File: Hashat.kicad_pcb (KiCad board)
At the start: 2 copper layers, 65 x 56.5 mm, 101 parts, among them IC1 BM1397_mode1, J1 Raspberry_Pi_2_3, J2 Conn_01x04, J3 Conn_01x05, J4 PJ-202AH, U1 EMC2101, U10 SN74AXC1T45DBVR, U3 DS4432U+, U4 25MHz, U5 SN74AXC1T45DBVR, U6 MCP1824T-1802E, U7 MCP1824T-0802E, U8 SN74AXC1T45DBVR, U9 SN74AXC1T45DBVR

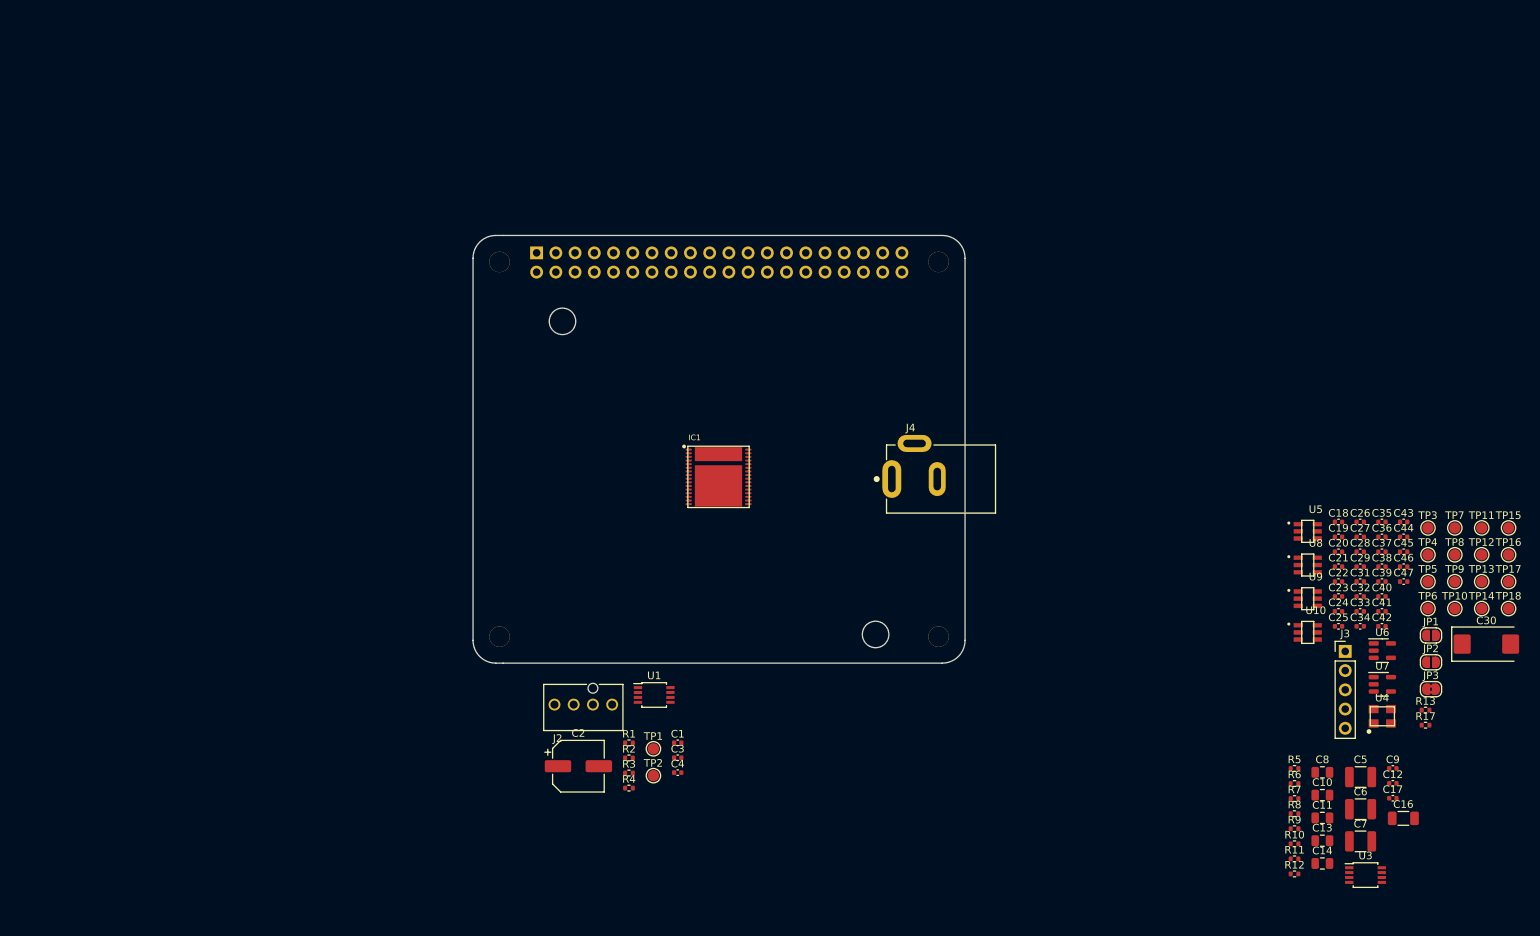
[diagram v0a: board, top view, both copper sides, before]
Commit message: cleared up some part reference designator madness
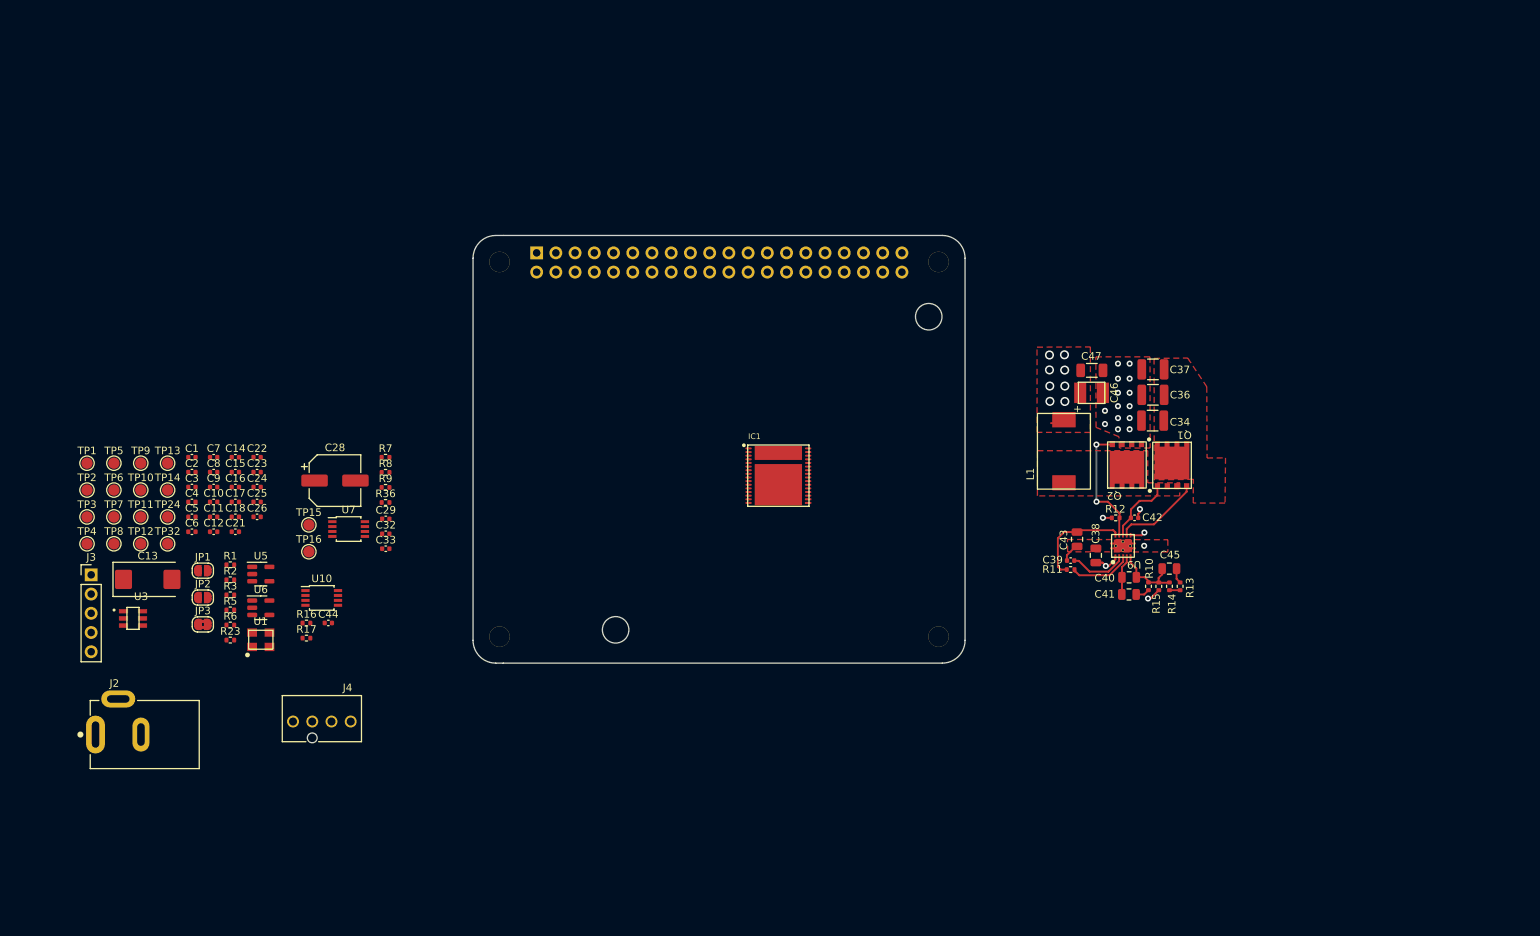
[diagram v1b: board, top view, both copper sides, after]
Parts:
- removed C19, C20, C27, C31, C35: 587-5514-1-ND, Capacitor_SMD:C_0402_1005Metric
- removed C30: 330uF, Capacitor_Tantalum_SMD:CP_EIA-7343-31_Kemet-D_Pad2.25x2.55mm_HandSolder
- removed R4: 10k, Resistor_SMD:R_0402_1005Metric
- removed TP17, TP18: TestPoint, TestPoint:TestPoint_Pad_D1.5mm
- removed U4: 25MHz, bitaxe:O 25,0-JO32-B-1V3-1-T1-LF
- removed U8: SN74AXC1T45DBVR, bitaxe:SN74AXC1T45
- added C15: 587-5514-1-ND, Capacitor_SMD:C_0402_1005Metric, F.Cu at (45.6, 86.8)
- added L1: 150nH, TPS40305_supply:FP1005R1-R15-R, F.Cu at (155.1, 84.0)
- added Q1: CSD17311Q5, TPS40305_supply:CSD17311Q5, F.Cu at (169.3, 85.9)
- added Q2: CSD17311Q5, TPS40305_supply:CSD17311Q5, F.Cu at (163.4, 85.8)
- added R14: 4.99k, Resistor_SMD:R_0402_1005Metric, F.Cu at (169.0, 101.9)
- added R15: 3.32k, Resistor_SMD:R_0402_1005Metric, F.Cu at (167.6, 101.9)
- added R16: 80k, Resistor_SMD:R_0402_1005Metric, F.Cu at (55.0, 106.7)
- added R23: 0, Resistor_SMD:R_0402_1005Metric, F.Cu at (44.9, 109.0)
- added R36: 10k, Resistor_SMD:R_0402_1005Metric, F.Cu at (65.4, 90.8)
- added TP24: TestPoint, TestPoint:TestPoint_Pad_D1.5mm, F.Cu at (36.7, 92.7)
- added TP32: TestPoint, TestPoint:TestPoint_Pad_D1.5mm, F.Cu at (36.7, 96.2)
- C1: value 470pF -> 311-3342-1-ND
- C10: value 180pF -> 587-5514-1-ND; footprint Capacitor_SMD:C_0805_2012Metric -> Capacitor_SMD:C_0402_1005Metric
- C11: value 1.5nF -> 587-5514-1-ND; footprint Capacitor_SMD:C_0805_2012Metric -> Capacitor_SMD:C_0402_1005Metric
- C12: value 0.1uF -> 587-5514-1-ND
- C13: value 10uF -> 330uF; footprint Capacitor_SMD:C_0805_2012Metric -> Capacitor_Tantalum_SMD:CP_EIA-7343-31_Kemet-D_Pad2.25x2.55mm_HandSolder
- C14: value 470pF -> 587-5514-1-ND; footprint Capacitor_SMD:C_0805_2012Metric -> Capacitor_SMD:C_0402_1005Metric
- C16: value 100uF -> 587-5514-1-ND; footprint Capacitor_SMD:C_1206_3216Metric -> Capacitor_SMD:C_0402_1005Metric
- C17: value 1uF -> 587-5514-1-ND
- C18, C3, C4: value 311-3342-1-ND -> 587-5514-1-ND
- C2: value 220uF -> 587-5514-1-ND; footprint Capacitor_SMD:CP_Elec_6.3x7.7 -> Capacitor_SMD:C_0402_1005Metric
- C21, C22, C23, C29, C33: value 587-5514-1-ND -> 311-3342-1-ND
- C24, C44: value 311-3342-1-ND -> 1uF
- C25: value 587-5514-1-ND -> 1uF
- C28: value 587-5514-1-ND -> 220uF; footprint Capacitor_SMD:C_0402_1005Metric -> Capacitor_SMD:CP_Elec_6.3x7.7
- C32: value 587-5514-1-ND -> 470pF
- C34: value 587-5514-1-ND -> 47uF; footprint Capacitor_SMD:C_0402_1005Metric -> Capacitor_SMD:C_1210_3225Metric
- C36, C37: value 311-3342-1-ND -> 47uF; footprint Capacitor_SMD:C_0402_1005Metric -> Capacitor_SMD:C_1210_3225Metric
- C38: value 311-3342-1-ND -> 1uF; footprint Capacitor_SMD:C_0402_1005Metric -> Capacitor_SMD:C_0805_2012Metric
- C39: value 311-3342-1-ND -> 3.3nF
- C40: value 1uF -> 180pF; footprint Capacitor_SMD:C_0402_1005Metric -> Capacitor_SMD:C_0805_2012Metric
- C41: value 1uF -> 1.5nF; footprint Capacitor_SMD:C_0402_1005Metric -> Capacitor_SMD:C_0805_2012Metric
- C42: value 311-3342-1-ND -> 0.1uF
- C43: value 311-3342-1-ND -> 10uF; footprint Capacitor_SMD:C_0402_1005Metric -> Capacitor_SMD:C_0805_2012Metric
- C45: value 311-3342-1-ND -> 470pF; footprint Capacitor_SMD:C_0402_1005Metric -> Capacitor_SMD:C_0805_2012Metric
- C46: value 311-3342-1-ND -> 220uF; footprint Capacitor_SMD:C_0402_1005Metric -> TPS40305_supply:CAP_2R5TPE220MAFB
- C47: value 311-3342-1-ND -> 100uF; footprint Capacitor_SMD:C_0402_1005Metric -> Capacitor_SMD:C_1206_3216Metric
- C5, C6: value 47uF -> 587-5514-1-ND; footprint Capacitor_SMD:C_1210_3225Metric -> Capacitor_SMD:C_0402_1005Metric
- C7: value 47uF -> 311-3342-1-ND; footprint Capacitor_SMD:C_1210_3225Metric -> Capacitor_SMD:C_0402_1005Metric
- C8: value 1uF -> 587-5514-1-ND; footprint Capacitor_SMD:C_0805_2012Metric -> Capacitor_SMD:C_0402_1005Metric
- C9: value 3.3nF -> 311-3342-1-ND
- J2: value Conn_01x04 -> PJ-202AH; footprint bitaxe:470531000 -> bitaxe:CUI_PJ-202AH
- J4: value PJ-202AH -> Conn_01x04; footprint bitaxe:CUI_PJ-202AH -> bitaxe:470531000
- R1: value 100 -> 1k
- R10: value 3.32k -> 3.83k
- R11: value 80k -> 100k
- R12: value DNP -> 4.12k
- R13: value 1k -> 1.33k
- R17: value 10k -> DNP
- R2: value 100 -> 0
- R3: value 10k -> 0
- R5: value 3.83k -> 0
- R6: value 100k -> 10k
- R7: value 4.12k -> 100
- R8: value 1.33k -> 100
- R9: value 4.99k -> 10k
- U1: value EMC2101 -> 25MHz; footprint Package_SO:TSSOP-8_3x3mm_P0.65mm -> bitaxe:O 25,0-JO32-B-1V3-1-T1-LF
- U10: value SN74AXC1T45DBVR -> DS4432U+; footprint bitaxe:SN74AXC1T45 -> Package_SO:TSSOP-8_3x3mm_P0.65mm
- U3: value DS4432U+ -> SN74AXC1T45DBVR; footprint Package_SO:TSSOP-8_3x3mm_P0.65mm -> bitaxe:SN74AXC1T45
- U5: value SN74AXC1T45DBVR -> MCP1824T-1802E; footprint bitaxe:SN74AXC1T45 -> Package_TO_SOT_SMD:SOT-23-5
- U6: value MCP1824T-1802E -> MCP1824T-0802E
- U7: value MCP1824T-0802E -> EMC2101; footprint Package_TO_SOT_SMD:SOT-23-5 -> Package_SO:TSSOP-8_3x3mm_P0.65mm
- U9: value SN74AXC1T45DBVR -> TPS40305; footprint bitaxe:SN74AXC1T45 -> TPS40305_supply:TPS40305
- moved TP11 177.2 mm to (33.1, 92.7)
- moved TP12 177.2 mm to (33.1, 96.2)
- moved TP3 177.2 mm to (26.0, 92.7)
- moved TP4 177.2 mm to (26.0, 96.2)
- moved TP7 177.2 mm to (29.6, 92.7)
- moved TP8 177.2 mm to (29.6, 96.2)
- moved TP13 174.3 mm to (36.7, 85.6)
- moved TP14 174.3 mm to (36.7, 89.1)
- moved TP5 174.3 mm to (29.6, 85.6)
- moved TP6 174.3 mm to (29.6, 89.1)
- moved TP10 174.3 mm to (33.1, 89.1)
- moved TP9 174.3 mm to (33.1, 85.6)
- moved U3 166.3 mm to (32.1, 106.1)
- moved J3 166.0 mm to (26.6, 100.3)
- moved JP1 162.5 mm to (41.3, 99.8)
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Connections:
- C1 pad 1: Net-(U1-DP) -> GND
- C1 pad 2: Net-(U1-DN) -> /BM1397/1V8
- C10 pad 1: Net-(U2-COMP) -> /BM1397/VDD
- C10 pad 2: /Power/OUT0 -> GND
- C11 pad 1: Net-(U2-COMP) -> /BM1397/VDD
- C11 pad 2: Net-(C11-Pad2) -> GND
- C12 pad 1: Net-(U2-BOOT) -> /BM1397/VDD
- C12 pad 2: /Power/SW -> Net-(IC1-VDD3_1)
- C13 pad 1: Net-(U2-BP) -> /BM1397/VDD
- C14 pad 1: Net-(C14-Pad1) -> /BM1397/1V8
- C14 pad 2: /Power/OUT0 -> GND
- C16 pad 1: /BM1397/VDD -> /BM1397/0V8
- C17 pad 1: /3V3 -> Net-(IC1-VDD2_1)
- C17 pad 2: GND -> Net-(IC1-VDD1_1)
- C18 pad 1: GND -> Net-(IC1-VDD1_1)
- C18 pad 2: /BM1397/1V8 -> GND
- C2 pad 1: /5V -> GND
- C2 pad 2: GND -> Net-(IC1-VDD1_0)
- C21 pad 1: /BM1397/0V8 -> /BM1397/1V8
- C22 pad 1: /BM1397/1V8 -> /5V
- C23 pad 1: Net-(IC1-VDD2_0) -> /5V
- C23 pad 2: Net-(IC1-VDD3_0) -> GND
- C24 pad 1: /BM1397/VDD -> /BM1397/1V8
- C25 pad 1: Net-(IC1-VDD3_0) -> /BM1397/0V8
- C25 pad 2: /BM1397/VDD -> GND
- C26 pad 1: /BM1397/VDD -> /BM1397/3V3
- C28 pad 1: /BM1397/VDD -> /5V
- C29 pad 1: /BM1397/VDD -> /5V
- C29 pad 2: Net-(IC1-VDD3_1) -> GND
- C3 pad 1: /5V -> Net-(IC1-VDD1_0)
- C3 pad 2: GND -> Net-(IC1-VDD2_0)
- C32 pad 1: /BM1397/1V8 -> Net-(U7-DP)
- C32 pad 2: GND -> Net-(U7-DN)
- C33 pad 1: /BM1397/0V8 -> /3V3
- C34 pad 1: Net-(IC1-VDD2_1) -> /5V
- C34 pad 2: Net-(IC1-VDD1_1) -> GND
- C36 pad 1: /BM1397/1V8 -> /5V
- C37 pad 1: /BM1397/3V3 -> /5V
- C39 pad 1: /5V -> Net-(U9-SS)
- C4 pad 1: /3V3 -> /BM1397/0V8
- C40 pad 1: /BM1397/1V8 -> Net-(U9-COMP)
- C40 pad 2: GND -> /Power/OUT0
- C41 pad 1: /BM1397/0V8 -> Net-(U9-COMP)
- C41 pad 2: GND -> Net-(C41-Pad2)
- C42 pad 1: /BM1397/1V8 -> Net-(U9-BOOT)
- C42 pad 2: GND -> /Power/SW
- C43 pad 1: /BM1397/3V3 -> Net-(U9-BP)
- C44 pad 1: /BM1397/1V8 -> /3V3
- C45 pad 1: /BM1397/3V3 -> Net-(C45-Pad1)
- C45 pad 2: GND -> /Power/OUT0
- C46 pad 1: /BM1397/1V8 -> /BM1397/VDD
- C47 pad 1: /BM1397/3V3 -> /BM1397/VDD
- C5 pad 1: /5V -> /BM1397/1V8
- C6 pad 1: /5V -> Net-(IC1-VDD2_0)
- C6 pad 2: GND -> Net-(IC1-VDD3_0)
- C7 pad 1: /5V -> /BM1397/VDD
- C8 pad 1: /5V -> Net-(IC1-VDD3_0)
- C8 pad 2: GND -> /BM1397/VDD
- C9 pad 1: Net-(U2-SS) -> /BM1397/VDD
- IC1 pad 10: /BM1397/BM_RO -> Net-(IC1-RO)
- IC1 pad 11: /BM1397/BM_CI -> Net-(IC1-CI)
- IC1 pad 12: Net-(IC1-CLKI) -> /BM1397/BM_CLKI
- IC1 pad 9: /BM1397/BM_RST_N -> /BM1397/RST_N
- J1 pad 10: /BM1397/RO -> /RPi/RO
- J1 pad 11: /BM1397/RST -> /RPi/RST
- J1 pad 36: /BM1397/BI -> /RPi/BI
- J1 pad 8: /BM1397/CI -> /RPi/CI
- J2 pad 1: GND -> /5V
- J2 pad 2: /5V -> GND
- J2 pad 3: /Fan/FAN_TACH -> GND
- J4 pad 1: /5V -> GND
- J4 pad 2: GND -> /5V
- J4 pad 3: GND -> /Fan/FAN_TACH
- R1 pad 1: Net-(U1-DN) -> GND
- R1 pad 2: /BM1397/TEMP_N -> /BM1397/RST_N
- R10 pad 1: /Power/OUT0 -> Net-(C41-Pad2)
- R10 pad 2: GND -> /Power/OUT0
- R11 pad 1: Net-(U3-FS0) -> /Power/PGOOD
- R11 pad 2: GND -> Net-(U9-BP)
- R12 pad 1: Net-(U3-FS1) -> Net-(Q2-G)
- R13 pad 1: GND -> /BM1397/VDD
- R13 pad 2: /BM1397/BM_RST_N -> Net-(C45-Pad1)
- R17 pad 1: Net-(IC1-RI) -> Net-(U10-FS1)
- R17 pad 2: /BM1397/1V8 -> GND
- R2 pad 1: /BM1397/TEMP_P -> Net-(U1-OUT)
- R2 pad 2: Net-(U1-DP) -> /BM1397/BM_CLKI
- R3 pad 1: /Fan/FAN_TACH -> /BM1397/RO
- R3 pad 2: /3V3 -> Net-(IC1-RO)
- R5 pad 1: Net-(C11-Pad2) -> /BM1397/CI
- R5 pad 2: /Power/OUT0 -> Net-(IC1-CI)
- R6 pad 1: /Power/PGOOD -> Net-(IC1-RI)
- R6 pad 2: Net-(U2-BP) -> /BM1397/1V8
- R7 pad 1: Net-(Q2-G) -> Net-(U7-DN)
- R7 pad 2: GND -> /BM1397/TEMP_N
- R8 pad 1: /BM1397/VDD -> /BM1397/TEMP_P
- R8 pad 2: Net-(C14-Pad1) -> Net-(U7-DP)
- R9 pad 1: /BM1397/VDD -> /Fan/FAN_PWM
- R9 pad 2: /Power/OUT0 -> /3V3
- TP1 pad 1: /Fan/FAN_TACH -> Net-(U1-OUT)
- TP10 pad 1: Net-(IC1-NRSTO) -> Net-(IC1-PIN_MODE)
- TP11 pad 1: Net-(IC1-CO) -> /BM1397/TEMP_P
- TP12 pad 1: Net-(IC1-CLKO) -> /BM1397/TEMP_N
- TP13 pad 1: Net-(IC1-PIN_MODE) -> /BM1397/1V8
- TP14 pad 1: Net-(IC1-RI) -> /BM1397/0V8
- TP15 pad 1: /BM1397/TEMP_P -> /Fan/FAN_PWM
- TP16 pad 1: /BM1397/TEMP_N -> /Fan/FAN_TACH
- TP2 pad 1: /Fan/FAN_PWM -> /BM1397/CI
- TP3 pad 1: Net-(IC1-CLKI) -> /BM1397/RO
- TP4 pad 1: /BM1397/CI -> /BM1397/RST_N
- TP5 pad 1: /BM1397/RO -> GND
- TP6 pad 1: /BM1397/RST_N -> Net-(IC1-BO)
- TP7 pad 1: GND -> Net-(IC1-NRSTO)
- TP8 pad 1: /BM1397/BM_BI -> Net-(IC1-CO)
- TP9 pad 1: Net-(IC1-BO) -> Net-(IC1-CLKO)
- U1 pad 1: /3V3 -> /BM1397/1V8
- U1 pad 2: Net-(U1-DP) -> GND
- U1 pad 3: Net-(U1-DN) -> Net-(U1-OUT)
- U1 pad 4: /Fan/FAN_PWM -> /BM1397/1V8
- U10 pad 1: /BM1397/1V8 -> /Fan/SDA
- U10 pad 2: GND -> /Fan/SCL
- U10 pad 3: /BM1397/BM_BI -> Net-(U10-FS1)
- U10 pad 4: /BM1397/BI -> GND
- U10 pad 5: GND -> Net-(U10-FS0)
- U10 pad 6: /BM1397/3V3 -> /Power/OUT0
- U3 pad 1: /Fan/SDA -> /BM1397/1V8
- U3 pad 2: /Fan/SCL -> GND
- U3 pad 3: Net-(U3-FS1) -> Net-(U3-A)
- U3 pad 4: GND -> /BM1397/CLKI
- U3 pad 5: Net-(U3-FS0) -> GND
- U3 pad 6: /Power/OUT0 -> /BM1397/3V3
- U5 pad 1: /BM1397/1V8 -> /5V
- U5 pad 3: /BM1397/BM_RST_N -> /5V
- U5 pad 4: /BM1397/RST -> unconnected-(U5-PG-Pad4)
- U5 pad 5: GND -> /BM1397/1V8
- U6 pad 5: /BM1397/1V8 -> /BM1397/0V8
- U7 pad 1: /5V -> /3V3
- U7 pad 2: GND -> Net-(U7-DP)
- U7 pad 3: /5V -> Net-(U7-DN)
- U7 pad 4: unconnected-(U7-PG-Pad4) -> /Fan/FAN_PWM
- U7 pad 5: /BM1397/0V8 -> GND
- U9 pad 1: /BM1397/1V8 -> /5V
- U9 pad 2: GND -> Net-(U9-SS)
- U9 pad 3: /BM1397/BM_CI -> /Power/PGOOD
- U9 pad 4: /BM1397/CI -> Net-(U9-COMP)
- U9 pad 5: GND -> /Power/OUT0
- U9 pad 6: /BM1397/3V3 -> Net-(U9-BOOT)
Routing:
- net Net-(Q2-G): track 0.00 -> 16.3 mm, vias 0 -> 2
- net Net-(U9-BP): track 0.00 -> 13.6 mm
- net Net-(Q1-G): track 0.00 -> 11.5 mm
- net /Power/OUT0: track 0.00 -> 9.84 mm
- net /Power/SW: track 0.00 -> 9.30 mm
- net /Power/PGOOD: track 0.00 -> 8.53 mm
- net Net-(U9-SS): track 0.00 -> 7.78 mm
- net GND: track 0.00 -> 5.60 mm, vias 0 -> 17
- net Net-(U9-COMP): track 0.00 -> 5.29 mm
- net /5V: track 0.00 -> 3.50 mm, vias 0 -> 1
- net /BM1397/VDD: track 0.00 -> 3.36 mm
- net Net-(U9-BOOT): track 0.00 -> 3.22 mm, vias 0 -> 2
- net Net-(C45-Pad1): track 0.00 -> 2.03 mm
- net Net-(C41-Pad2): track 0.00 -> 1.86 mm
- net (no net): vias 0 -> 8
- added copper zone on F.Cu, net /5V
- added copper zone on F.Cu, net /BM1397/VDD
- added copper zone on F.Cu, net /Power/SW
- added copper zone on F.Cu, net GND

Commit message: swapped out the VCCIO LDOs for some LCSC versions
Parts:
- removed J2: PJ-202AH, bitaxe:CUI_PJ-202AH
- added DC1: DC-044K-D025, lcsc:DC-IN-TH_DC-044K-D025, F.Cu at (85.3, 68.1)
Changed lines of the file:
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@@
+    )
+  )
+  (footprint "lcsc:DC-IN-TH_DC-044K-D025" (layer "F.Cu")
+    (at 85.27 68.123)
+    (property "JLC Part" "Extended Part")
+    (property "LCSC Part" "C963204")
+    (property "Manufacturer" "G-Switch")
+    (property "Sheetfile" "/Users/skot/Work/Bitcoin/Hashat/Hashat.sch")
+    (property "Sheetname" "")
+    (attr smd)
+    (fp_text reference "DC1" (at 2.087 6.122) (layer "F.SilkS")
+        (effects (font (size 1 1) (thickness 0.15)))
+    )
+    (fp_text value "DC-044K-D025" (at 0 8.93) (layer "F.Fab")
+        (effects (font (size 1 1) (thickness 0.15)))
+    )
+    (fp_text user "${REFERENCE}" (at 0 0) (layer "F.Fab")
+        (effects (font (size 1 1) (thickness 0.15)))
+    )
+    (fp_line (start -8.28 -4.85) (end -7.36 -4.85)
+      (stroke (width 0.25) (type solid)) (layer "F.SilkS"))
+    (fp_line (start -8.28 -2.06) (end -8.28 -4.85)
+      (stroke (width 0.25) (type solid)) (layer "F.SilkS"))
+    (fp_line (start -8.28 -2.06) (end -8.28 1.11)
+      (stroke (width 0.25) (type solid)) (layer "F.SilkS"))
+    (fp_line (start -8.28 1.11) (end -8.28 4.93)
+      (stroke (width 0.25) (type solid)) (layer "F.SilkS"))
+    (fp_line (start -8.28 4.93) (end -7.36 4.93)
+      (stroke (width 0.25) (type solid)) (layer "F.SilkS"))
+    (fp_line (start -3.1 -4.85) (end 3.34 -4.85)
+      (stroke (width 0.25) (type solid)) (layer "F.SilkS"))
+    (fp_line (start -3.1 4.93) (end 3.34 4.93)
+      (stroke (width 0.25) (type solid)) (layer "F.SilkS"))
+    (fp_line (start 3.34 -4.85) (end 3.34 -4.24)
+      (stroke (width 0.25) (type solid)) (layer "F.SilkS"))
+    (fp_line (start 3.34 -3.41) (end 3.34 0.96)
+      (stroke (width 0.25) (type solid)) (layer "F.SilkS"))
+    (fp_line (start 3.34 1.79) (end 3.34 4.93)
+      (stroke (width 0.25) (type solid)) (layer "F.SilkS"))
+    (fp_circle (center 4.16 1.3) (end 4.31 1.3)
+      (stroke (width 0.3) (type solid)) (fill none) (layer "Cmts.User"))
+    (fp_circle (center -8.28 -5.12) (end -8.25 -5.12)
+      (stroke (width 0.06) (type solid)) (fill none) (layer "F.Fab"))
+    (fp_circle (center 5.23 1.2) (end 5.48 1.2)
+      (stroke (width 0.5) (type solid)) (fill none) (layer "F.Fab"))
+    (pad "" thru_hole circle (at -4.27 1.2) (size 2.5 2.5) (drill 2.5) (layers "*.Cu" "*.Mask"))
+    (pad "1" thru_hole oval (at -5.23 -4.93 90) (size 1.2 3.8) (drill oval 0.599999 2.999994) (layers "*.Cu" "*.Paste" "*.Mask")
+      (net 1 "GND") (pinfunction "1") (pintype "unspecified"))
+    (pad "2" thru_hole oval (at 1.98 -4 90) (size 1.2 2.5) (drill oval 0.599999 1.999996) (layers "*.Cu" "*.Paste" "*.Mask")
+      (net 1 "GND") (pinfunction "2") (pintype "unspecified"))
+    (pad "3" thru_hole oval (at 1.98 1.2 90) (size 1.2 2.5) (drill oval 0.599999 1.999996) (layers "*.Cu" "*.Paste" "*.Mask")
+      (net 1 "GND") (pinfunction "3") (pintype "unspecified"))
+    (pad "4" thru_hole circle (at 5.23 1.2 90) (size 2 2) (drill 1.300023) (layers "*.Cu" "*.Paste" "*.Mask")
+      (net 28 "/5V") (pinfunction "4") (pintype "unspecified"))
+    (pad "6" thru_hole oval (at -5.23 4.93 90) (size 1.2 3.8) (drill oval 0.599999 2.999994) (layers "*.Cu" "*.Paste" "*.Mask")
+      (net 1 "GND") (pinfunction "6") (pintype "unspecified"))
+    (model "/Users/skot/Documents/KiCad/easyeda2kicad/lcsc.3dshapes/DC-IN-TH_DC-044K-D025.wrl"
+      (offset (xyz -0.3 0.02 0))
+      (scale (xyz 1 1 1))
+      (rotate (xyz 0 0 0))
     )
   )
@@
       (net 54 "Net-(IC1-RI)") (pinfunction "1") (pintype "passive"))
   )
-  (footprint "bitaxe:CUI_PJ-202AH" (layer "F.Cu")
-    (at 33.627 121.435)
-    (property "DK" "CP-202AH-ND")
-    (property "PARTNO" "PJ-202AH")
-    (property "Sheetfile" "/Users/skot/Work/Bitcoin/Hashat/Hashat.sch")
-    (property "Sheetname" "")
-    (attr through_hole)
-    (fp_text reference "J2" (at -4.01529 -6.76551) (layer "F.SilkS")
-        (effects (font (size 1.000079 1.000079) (thickness 0.15)))
-    )
-    (fp_text value "PJ-202AH" (at 0.43048 5.781315) (layer "F.Fab")
-        (effects (font (size 1.001094 1.001094) (thickness 0.15)))
-    )
-    (fp_line (start -7.2 -4.5) (end -6.05 -4.5)
-      (stroke (width 0.127) (type solid)) (layer "F.SilkS"))
-    (fp_line (start -7.2 -2.55) (end -7.2 -4.5)
-      (stroke (width 0.127) (type solid)) (layer "F.SilkS"))
-    (fp_line (start -7.2 4.5) (end -7.2 2.65)
-      (stroke (width 0.127) (type solid)) (layer "F.SilkS"))
-    (fp_line (start -0.95 -4.5) (end 7.2 -4.5)
-      (stroke (width 0.127) (type solid)) (layer "F.SilkS"))
-    (fp_line (start 7.2 -4.5) (end 7.2 4.5)
-      (stroke (width 0.127) (type solid)) (layer "F.SilkS"))
-    (fp_line (start 7.2 4.5) (end -7.2 4.5)
-      (stroke (width 0.127) (type solid)) (layer "F.SilkS"))
-    (fp_circle (center -8.5 0) (end -8.3 0)
-      (stroke (width 0.4) (type solid)) (fill none) (layer "F.SilkS"))
-    (fp_line (start -8.05 -2.25) (end -8.05 2.35)
-      (stroke (width 0.05) (type solid)) (layer "F.CrtYd"))
-    (fp_line (start -8.05 2.35) (end -7.45 2.35)
-      (stroke (width 0.05) (type solid)) (layer "F.CrtYd"))
-    (fp_line (start -7.45 -4.75) (end -6.05 -4.75)
-      (stroke (width 0.05) (type solid)) (layer "F.CrtYd"))
-    (fp_line (start -7.45 -2.25) (end -8.05 -2.25)
-      (stroke (width 0.05) (type solid)) (layer "F.CrtYd"))
-    (fp_line (start -7.45 -2.25) (end -7.45 -4.75)
-      (stroke (width 0.05) (type solid)) (layer "F.CrtYd"))
-    (fp_line (start -7.45 4.75) (end -7.45 2.35)
-      (stroke (width 0.05) (type solid)) (layer "F.CrtYd"))
-    (fp_line (start -6.05 -6.1) (end -0.95 -6.1)
-      (stroke (width 0.05) (type solid)) (layer "F.CrtYd"))
-    (fp_line (start -6.05 -4.75) (end -6.05 -6.1)
-      (stroke (width 0.05) (type solid)) (layer "F.CrtYd"))
-    (fp_line (start -0.95 -6.1) (end -0.95 -4.75)
-      (stroke (width 0.05) (type solid)) (layer "F.CrtYd"))
-    (fp_line (start -0.95 -4.75) (end 7.5 -4.75)
-      (stroke (width 0.05) (type solid)) (layer "F.CrtYd"))
-    (fp_line (start 7.5 -4.75) (end 7.5 4.75)
-      (stroke (width 0.05) (type solid)) (layer "F.CrtYd"))
-    (fp_line (start 7.5 4.75) (end -7.45 4.75)
-      (stroke (width 0.05) (type solid)) (layer "F.CrtYd"))
-    (fp_line (start -7.2 -4.5) (end 7.2 -4.5)
-      (stroke (width 0.127) (type solid)) (layer "F.Fab"))
-    (fp_line (start -7.2 4.5) (end -7.2 -4.5)
-      (stroke (width 0.127) (type solid)) (layer "F.Fab"))
-    (fp_line (start 7.2 -4.5) (end 7.2 4.5)
-      (stroke (width 0.127) (type solid)) (layer "F.Fab"))
-    (fp_line (start 7.2 4.5) (end -7.2 4.5)
-      (stroke (width 0.127) (type solid)) (layer "F.Fab"))
-    (pad "1" thru_hole oval (at -6.5 0) (size 2.5 5) (drill oval 1 3.5) (layers "*.Cu" "*.Mask")
-      (net 28 "/5V") (pintype "passive"))
-    (pad "2" thru_hole oval (at -0.5 0) (size 2.25 4.5) (drill oval 1 3) (layers "*.Cu" "*.Mask")
-      (net 1 "GND") (pintype "passive"))
-    (pad "3" thru_hole oval (at -3.5 -4.7) (size 4.5 2.25) (drill oval 3 1) (layers "*.Cu" "*.Mask")
-      (net 1 "GND") (pintype "passive"))
-  )
   (footprint "bitaxe:470531000" (layer "F.Cu")
